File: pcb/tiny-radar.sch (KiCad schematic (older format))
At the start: 0 parts

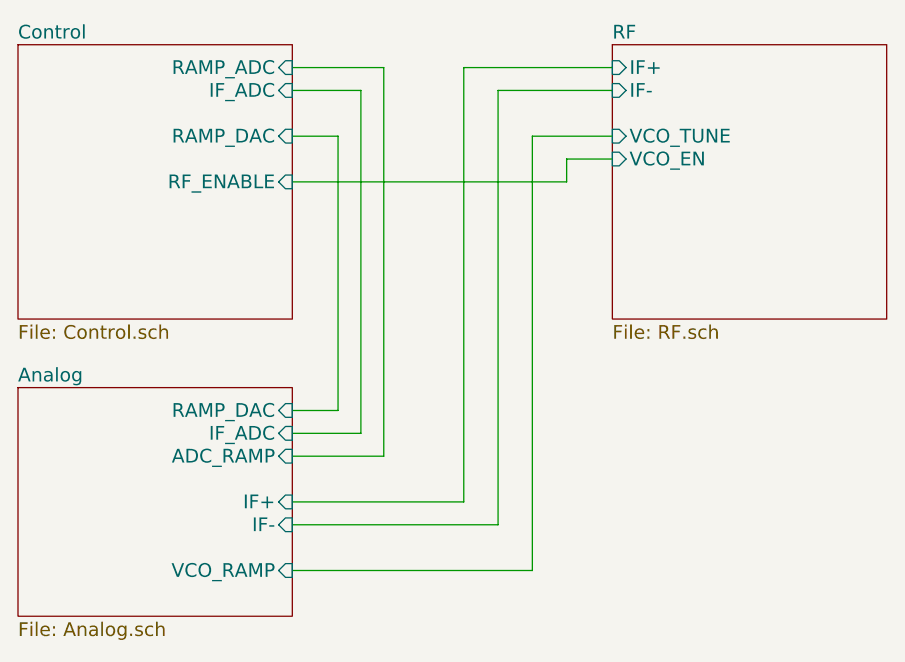
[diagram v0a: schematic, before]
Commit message: new uc and added AGC. Sent off to fab
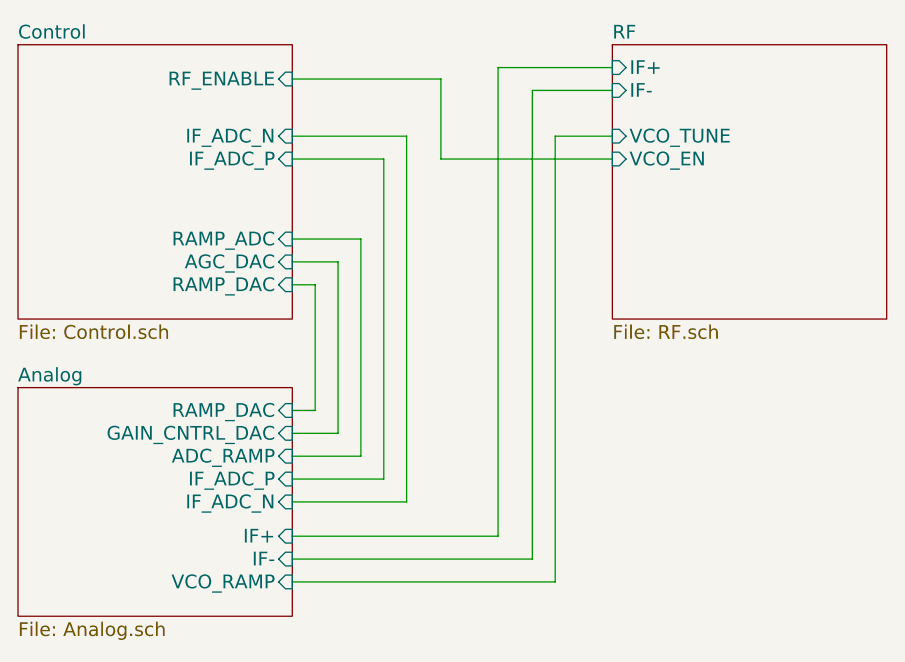
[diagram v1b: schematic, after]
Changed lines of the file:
@@
 F0 "Control" 60
 F1 "Control.sch" 60
-F2 "RAMP_ADC" I R 2900 2000 60
-F3 "IF_ADC" I R 2900 2100 60
-F4 "RAMP_DAC" I R 2900 2300 60
-F5 "RF_ENABLE" I R 2900 2500 60
+F2 "RAMP_ADC" I R 2900 2750 60
+F3 "IF_ADC_P" I R 2900 2400 60
+F4 "RAMP_DAC" I R 2900 2950 60
+F5 "RF_ENABLE" I R 2900 2050 60
+F6 "IF_ADC_N" I R 2900 2300 60
+F7 "AGC_DAC" I R 2900 2850 60
 $EndSheet
 $Sheet
@@
 F0 "Analog" 60
 F1 "Analog.sch" 60
-F2 "IF+" I R 2900 3900 60
-F3 "IF-" I R 2900 4000 60
-F4 "RAMP_DAC" I R 2900 3500 60
-F5 "IF_ADC" I R 2900 3600 60
-F6 "VCO_RAMP" I R 2900 4200 60
-F7 "ADC_RAMP" I R 2900 3700 60
+F2 "RAMP_DAC" I R 2900 3500 60
+F3 "VCO_RAMP" I R 2900 4250 60
+F4 "ADC_RAMP" I R 2900 3700 60
+F5 "GAIN_CNTRL_DAC" I R 2900 3600 60
+F6 "IF_ADC_P" I R 2900 3800 60
+F7 "IF_ADC_N" I R 2900 3900 60
+F8 "IF+" I R 2900 4050 60
+F9 "IF-" I R 2900 4150 60
 $EndSheet
 $Sheet
@@
 $EndSheet
 Wire Wire Line
-	2900 2300 3100 2300
+	2900 2950 3000 2950
 Wire Wire Line
-	3100 2300 3100 3500
+	3000 2950 3000 3500
 Wire Wire Line
-	3100 3500 2900 3500
+	3000 3500 2900 3500
 Wire Wire Line
-	2900 2100 3200 2100
+	2900 2850 3100 2850
 Wire Wire Line
-	3200 2100 3200 3600
+	3100 2850 3100 3600
 Wire Wire Line
-	3200 3600 2900 3600
+	3100 3600 2900 3600
 Wire Wire Line
-	2900 2000 3300 2000
+	2900 2750 3200 2750
 Wire Wire Line
-	3300 2000 3300 3700
+	3200 2750 3200 3700
 Wire Wire Line
-	3300 3700 2900 3700
+	3200 3700 2900 3700
 Wire Wire Line
-	2900 3900 3650 3900
+	2900 2400 3300 2400
 Wire Wire Line
-	3650 3900 3650 2000
+	3300 2400 3300 3800
 Wire Wire Line
-	3650 2000 4300 2000
+	3300 3800 2900 3800
 Wire Wire Line
-	2900 4000 3800 4000
+	2900 2300 3400 2300
 Wire Wire Line
-	3800 4000 3800 2100
+	3400 2300 3400 3900
 Wire Wire Line
-	3800 2100 4300 2100
+	3400 3900 2900 3900
 Wire Wire Line
-	2900 4200 3950 4200
+	2900 4050 3800 4050
 Wire Wire Line
-	3950 4200 3950 2300
+	3800 4050 3800 2000
 Wire Wire Line
-	3950 2300 4300 2300
+	3800 2000 4300 2000
 Wire Wire Line
-	4300 2400 4100 2400
+	2900 4150 3950 4150
 Wire Wire Line
-	4100 2400 4100 2500
+	3950 4150 3950 2100
 Wire Wire Line
-	4100 2500 2900 2500
+	3950 2100 4300 2100
+Wire Wire Line
+	2900 4250 4050 4250
+Wire Wire Line
+	4050 4250 4050 2300
+Wire Wire Line
+	4050 2300 4300 2300
+Wire Wire Line
+	4300 2400 3550 2400
+Wire Wire Line
+	3550 2400 3550 2050
+Wire Wire Line
+	3550 2050 2900 2050
 $EndSCHEMATC
